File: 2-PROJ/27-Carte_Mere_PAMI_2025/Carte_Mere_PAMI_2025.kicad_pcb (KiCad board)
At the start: 2 copper layers, 212.2 x 114.8 mm, 114 parts, among them J1 Conn_01x03, J10 Conn_01x04, J11 Conn_01x03, J12 Conn_01x03, J13 Conn_01x03, J14 Conn_01x03, J15 3.5mm WR-TBL, J16 Conn_01x04, J17 Conn_01x02, J18 Conn_01x02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

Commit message: préplacement carte PAMI 2025
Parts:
- removed the H1 at (216.0, 73.0)
- removed the H2 at (250.6, 73.0)
- removed the H3 at (268.7, 23.7)
- removed the H4 at (197.7, 23.7)
- removed the J1 at (242.1, 83.1)
- C22: footprint Capacitor_THT:C_Radial_D8.0mm_H11.5mm_P3.50mm -> Capacitor_THT:C_Radial_D6.3mm_H11.0mm_P2.50mm
- J10, J2, J9: moved to B.Cu
- J15, J7: value 3.5mm WR-TBL -> Conn_01x02; footprint ConnectorsEvo:691321100002 -> Connector_Wire:SolderWire-0.75sqmm_1x02_P4.8mm_D1.25mm_OD2.3mm; moved to B.Cu
- J17, J18, J19, J3: footprint Connector_PinHeader_2.54mm:PinHeader_1x03_P2.54mm_Vertical -> Connector_PinHeader_2.54mm:PinHeader_1x02_P2.54mm_Vertical
- J8: footprint Connector_PinHeader_2.54mm:PinHeader_1x04_P2.54mm_Vertical -> Carte_Mere_PAMI_2025:Ecran_OLED0.9_Waveshare
- SW1: footprint Connector_PinHeader_2.54mm:PinHeader_1x03_P2.54mm_Vertical -> Button_Switch_THT:SW_Slide_SPDT_Straight_CK_OS102011MS2Q
- moved C21 145.2 mm to (150.0, 132.5), turned to 90 degrees
- moved U5 138.7 mm to (150.7, 113.9)
- moved J13 130.7 mm to (133.5, 129.0)
- moved J14 129.2 mm to (136.1, 129.0)
- moved J10 128.9 mm to (147.7, 115.7)
- moved C25 127.9 mm to (140.0, 125.0), turned to 180 degrees
- moved R20 125.1 mm to (140.0, 123.5)
- moved R21 124.4 mm to (140.0, 122.0), turned to 180 degrees
- moved R22 123.8 mm to (140.0, 120.5), turned to 180 degrees
- moved C15 121.1 mm to (152.7, 117.9), turned to 180 degrees
- moved J16 118.6 mm to (140.0, 108.0)
- moved C20 117.3 mm to (115.0, 132.0), turned to 90 degrees
- moved C27 117.2 mm to (128.0, 132.5), turned to 90 degrees
- moved C9 114.3 mm to (129.0, 95.5), turned to 90 degrees
- moved C23 113.2 mm to (143.0, 131.0), turned to 90 degrees
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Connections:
- D1 pad 1: Net-(D1-K) -> GND
- D1 pad 2: +5P -> Net-(D1-A)
- J17 pad 1: /uSW1 -> GND
- J17 pad 2: GND -> /uSW1
- J18 pad 1: /uSW2 -> GND
- J18 pad 2: GND -> /uSW2
- J19 pad 1: /uSW3 -> GND
- J19 pad 2: GND -> /uSW3
- J2 pad 1: /ALIM_EN_5L -> +5L
- J2 pad 2: /EN_5L -> GND
- J2 pad 3: /CaptTOR_2 -> GND
- J2 pad 4: /CaptTOR_1 -> +5P
- J2 pad 5: +5P -> /CaptTOR_1
- J2 pad 6: GND -> /CaptTOR_2
- J2 pad 7: GND -> /EN_5L
- J2 pad 8: +5L -> /ALIM_EN_5L
- J3 pad 1: +5P -> Net-(D2-A)
- J3 pad 2: Net-(D2-A) -> +5P
- R1 pad 1: GND -> Net-(D1-A)
- R1 pad 2: Net-(D1-K) -> +5P
- SW1 pad 1: unconnected-(SW1-C-Pad1) -> /ALIM_EN_5L
- SW1 pad 3: /ALIM_EN_5L -> /EN_5L
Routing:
- removed copper zone on B.Cu, net (none)
- removed copper zone on F.Cu, net (none)
- removed copper zone on B.Cu, net GND
- removed copper zone on F.Cu, net GND
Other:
- board size 212.2 x 114.8 mm -> 100 x 77 mm

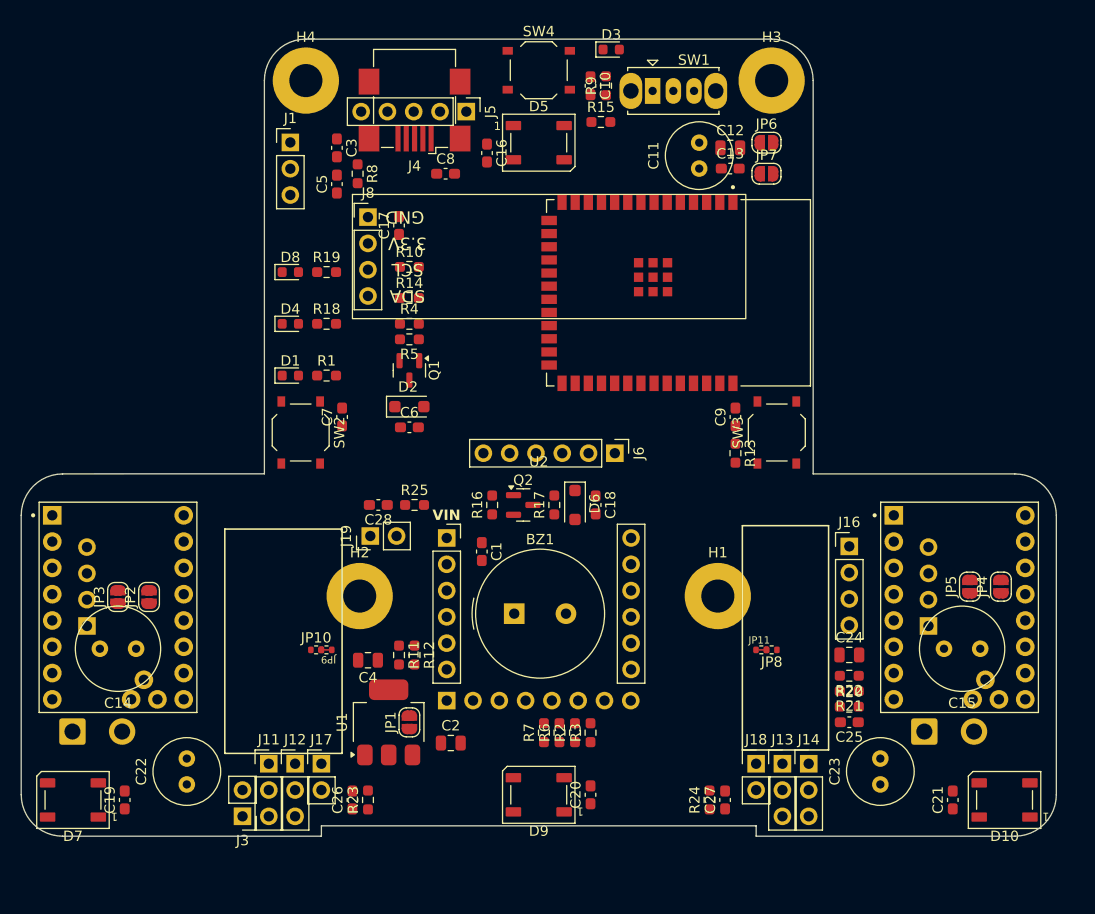
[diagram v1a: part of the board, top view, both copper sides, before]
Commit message: WIP routage avec ajout d'un AU_STATUS à la place de la LED statut
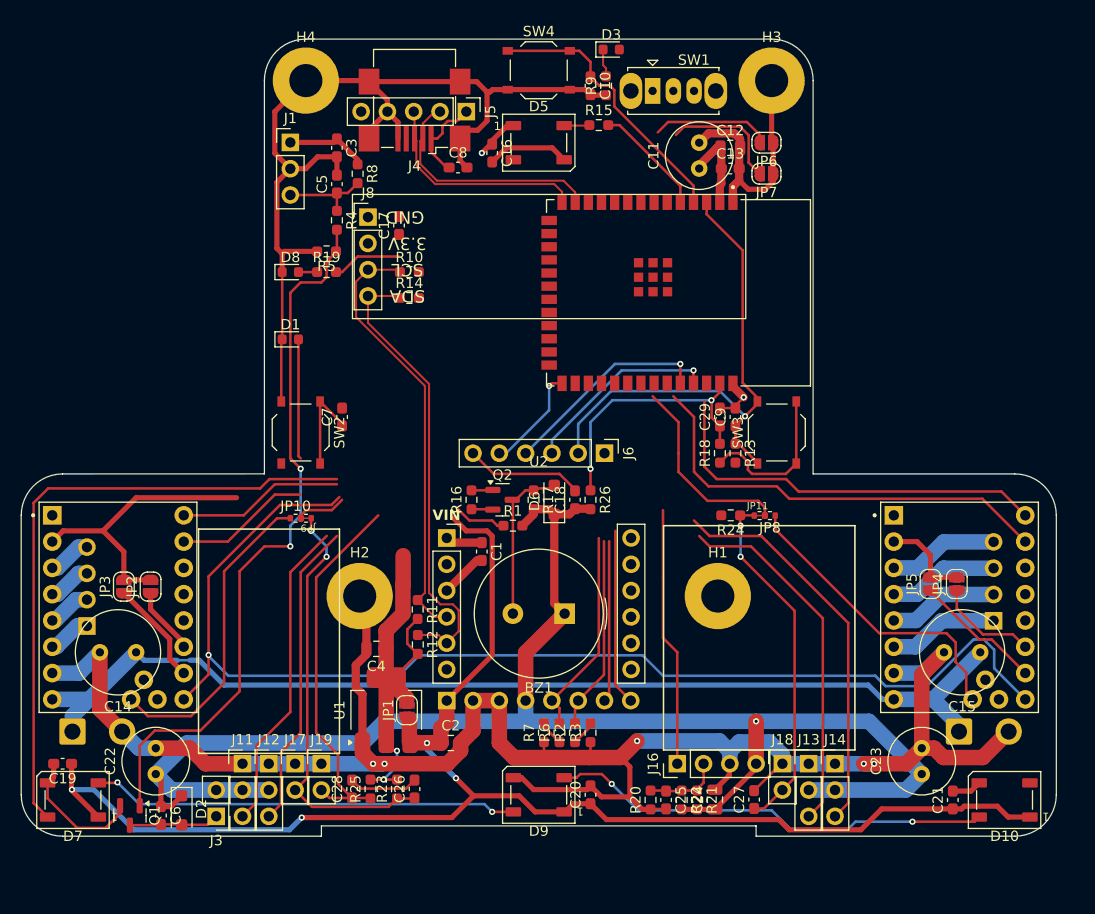
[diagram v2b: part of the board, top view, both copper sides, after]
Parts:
- removed D4: LED, LED_SMD:LED_0603_1608Metric
- added C29: 100nF, Capacitor_SMD:C_0603_1608Metric_Pad1.08x0.95mm_HandSolder, F.Cu at (127.5, 95.5)
- added R26: 10k, Resistor_SMD:R_0603_1608Metric_Pad0.98x0.95mm_HandSolder, F.Cu at (115.0, 103.5)
- J10, J9: footprint Connector_PinHeader_2.54mm:PinHeader_1x04_P2.54mm_Vertical -> Connector_PinHeader_2.54mm:PinHeader_1x04_P2.54mm_Horizontal
- R18: value 1K -> 10k
- moved Q1 50.8 mm to (70.5, 134.0)
- moved D2 44.8 mm to (75.5, 133.5), turned to -90 degrees
- moved C6 44.5 mm to (73.5, 134.0), turned to -90 degrees
- moved R18 40.0 mm to (127.5, 99.0), turned to 90 degrees
- moved R25 27.8 mm to (93.7, 131.4), turned to 90 degrees
- moved R24 27.6 mm to (128.5, 105.0), turned to 180 degrees
- moved C28 27.6 mm to (92.0, 131.4), turned to 90 degrees
- moved J16 26.8 mm to (123.4, 129.0), turned to 90 degrees
- moved R1 23.1 mm to (107.5, 106.0)
- moved J19 22.5 mm to (89.0, 129.0), turned to 0 degrees
- moved R20 21.2 mm to (120.8, 132.5), turned to 90 degrees
- moved R22 20.2 mm to (123.8, 132.5), turned to -90 degrees
- moved C25 19.2 mm to (122.3, 132.5), turned to -90 degrees
- moved C24 19.1 mm to (127.0, 132.5), turned to 90 degrees
- moved R21 18.1 mm to (125.3, 132.5), turned to -90 degrees
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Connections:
- net /LED_GREEN renamed /AU_STATUS
- R18 pad 1: Net-(D4-A) -> GND
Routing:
- net GND: track 0.00 -> 368.6 mm, vias 0 -> 6
- net +5P: track 0.00 -> 150.4 mm, vias 0 -> 1
- net +5L: track 0.00 -> 148.6 mm, vias 0 -> 5
- net /M_EN: track 0.00 -> 116.0 mm, vias 0 -> 1
- net VBATT_12V: track 0.00 -> 103.2 mm
- net +3.3V: track 0.00 -> 93.9 mm, vias 0 -> 2
- net Net-(Q1-G): track 0.00 -> 69.6 mm, vias 0 -> 2
- net /WS_2: track 0.00 -> 61.2 mm
- net /ESP32_EN: track 0.00 -> 50.5 mm, vias 0 -> 1
- net /SDA: track 0.00 -> 44.6 mm
- net /M2_STEP: track 0.00 -> 42.9 mm
- net /WS_4: track 0.00 -> 42.9 mm, vias 0 -> 2
- net /SCL: track 0.00 -> 42.1 mm
- net /WS_3: track 0.00 -> 41.3 mm, vias 0 -> 2
- net /uSW1: track 0.00 -> 40.7 mm, vias 0 -> 2
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
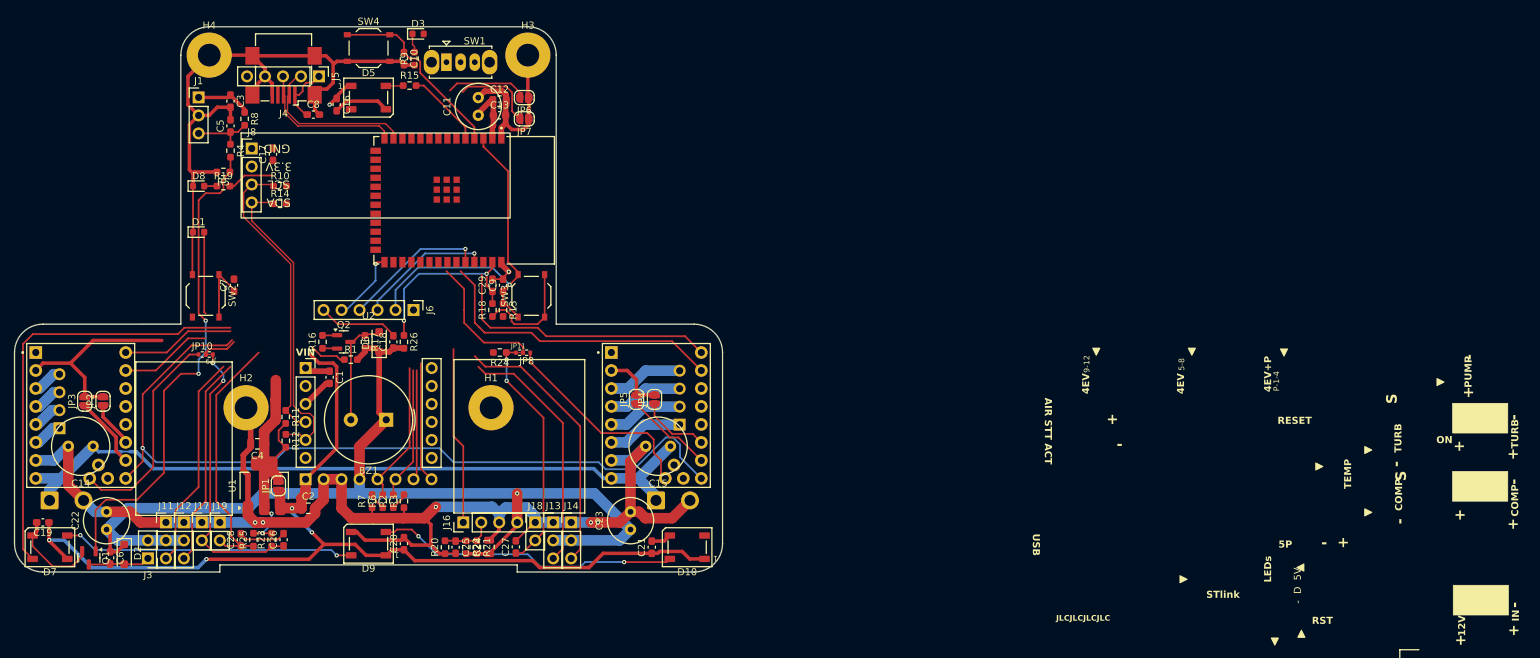
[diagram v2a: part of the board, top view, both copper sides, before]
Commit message: fin du routage carte PAMI 2025
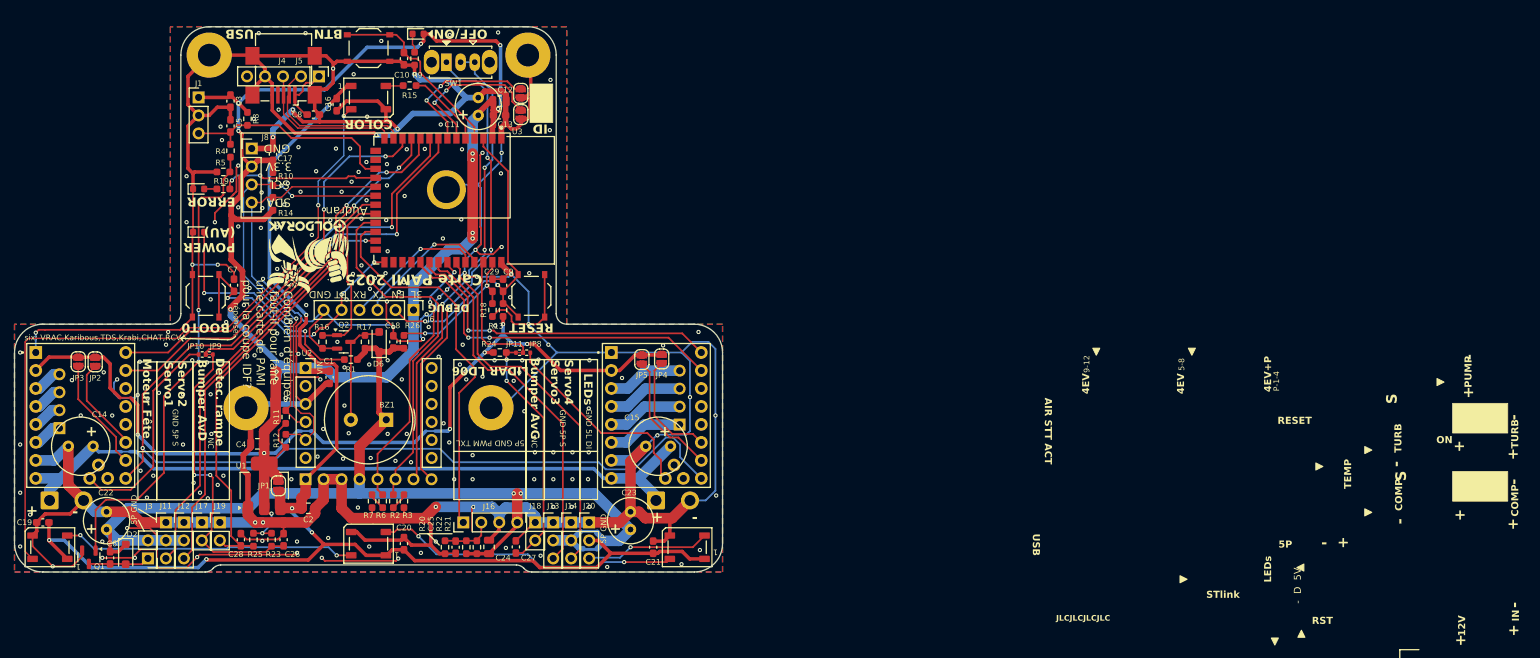
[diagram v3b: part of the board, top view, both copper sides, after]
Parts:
- added G***: LOGO, LOGO, F.Cu at (101.5, 92.5)
- added G***: LOGO, LOGO, F.Cu at (101.3, 87.1)
- added J20: Conn_01x03, Connector_PinHeader_2.54mm:PinHeader_1x03_P2.54mm_Vertical, F.Cu at (141.2, 129.0)
- moved JP4 5.82 mm to (151.4, 105.9)
- moved JP5 5.68 mm to (148.6, 106.0)
- moved JP2 5.68 mm to (71.4, 106.3)
- moved JP3 5.66 mm to (69.0, 106.3)
- moved R10 1.41 mm to (96.5, 80.5), turned to 90 degrees
- moved R14 1.00 mm to (96.5, 84.0), turned to -90 degrees
- moved JP6 0.78 mm to (131.5, 68.4), turned to 90 degrees
- moved JP7 0.78 mm to (131.5, 71.4), turned to 90 degrees
- moved D8 0.40 mm to (86.0, 81.9)
- moved R19 0.40 mm to (89.5, 81.9)
- moved R8 0.40 mm to (92.9, 72.0)
- moved D2 0.20 mm to (75.7, 133.5)
- moved C21 0.20 mm to (150.2, 132.5)
- moved Q1 0.08 mm to (70.5, 133.9)
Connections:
- D10 pad 2: unconnected-(D10-DOUT-Pad2) -> /WS_5
- U3 pad 18: /TX_LIDAR -> /LED_RED
- U3 pad 24: /M1_DIAG/uSW1 -> /TX_LIDAR
- U3 pad 38: /LED_RED -> /M2_DIAG/uSW2
- U3 pad 8: /M2_DIAG/uSW2 -> /M1_DIAG/uSW1
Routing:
- net GND: track 368.6 -> 790.3 mm, vias 6 -> 209
- net +3.3V: track 93.9 -> 346.7 mm, vias 2 -> 21
- net /EN_5L: track 15.6 -> 66.6 mm, vias 0 -> 3
- net /ALIM_EN_5L: track 17.0 -> 67.5 mm, vias 0 -> 3
- net /M1_DIAG/uSW1: track 4.90 -> 51.2 mm, vias 0 -> 2
- net +5L: track 148.6 -> 194.5 mm, vias 5 -> 6
- net /SERVO1: track 30.5 -> 76.0 mm, vias 0 -> 2
- net /M1_DIR: track 16.0 -> 59.8 mm, vias 0 -> 2
- net /SERVO2: track 29.8 -> 73.3 mm, vias 0 -> 2
- net /M_EN: track 116.0 -> 158.3 mm, vias 1 -> 3
- net /WS_2: track 61.2 -> 98.7 mm, vias 0 -> 2
- net /CaptTOR_2: track 18.7 -> 51.6 mm
- net /M1_STEP: track 13.2 -> 42.9 mm, vias 0 -> 2
- net /TX_LIDAR: track 25.1 -> 54.5 mm
- net /uSW3: track 36.3 -> 65.1 mm
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- added copper zone on B.Cu, net GND
- added copper zone on F.Cu, net GND
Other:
- outline, holes or cut-outs redrawn
- board text added: "3L EN TX RX BT GND"
- board text added: "5-36V"
- board text added: "5P GND"
- board text added: "5P GND PWM TXL"
- board text added: "<= Glory hole"
- board text added: "Audran"
- board text added: "BOOT0"
- board text added: "BTN"
- board text added: "Bumper AvD"
- board text added: "Bumper AvG"
- board text added: "COLOR"
- board text added: "Carte PAMI 2025"
- board text added: "Combien d'équipes faut-il pour faire une carte de PAMI pour la coupe IDF?"
- board text added: "DEBUG"
- board text added: "Detec. rampe"
- board text added: "EN_5L Cp2 Cp1 +5P GND GND +5L"
- board text added: "ERROR"
- board text added: "GND 5L DI"
- board text added: "GND 5P S"
- board text added: "ID"
- board text added: "LIDAR LD06"
- board text added: "M1B M1A M2A M2B"
- board text added: "MOT Droit"
- board text added: "MOT Gauche"
- board text added: "Moteur Fête"
- board text added: "NC"
- board text added: "OFF/ON"
- board text added: "POWER (AU)"
- board text added: "Servo2 Servo1"
- board text added: "Servo4 Servo3"
- board text added: "réponse:"
- board text added: "six: VRAC,Karibous,TDS,Krabi,CHAT,RCVA"
- board text removed: "Carte Pneumatique 2025"
- board text removed: "Mehdi, Raphael & Audran"

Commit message: modification de bouton et fichier de prod
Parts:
- added SW5: SW_Push, Button_Switch_SMD:SW_Push_1TS009xxxx-xxxx-xxxx_6x6x5mm, F.Cu at (86.9, 97.0)
- added SW6: SW_Push, Button_Switch_SMD:SW_Push_1TS009xxxx-xxxx-xxxx_6x6x5mm, F.Cu at (133.0, 97.0)
- added SW7: SW_Push, Button_Switch_SMD:SW_Push_1TS009xxxx-xxxx-xxxx_6x6x5mm, F.Cu at (110.0, 62.3)
- D1: value LED -> LED yellow
- D3: value LED -> LED green
- D8: value LED -> LED red
- R1, R17, R19, R9: value 1K -> 1k
- R10, R11, R12, R13, R14, R20, R21, R22, R23, R24, R25: value 10K -> 10k
- moved J9 0.53 mm to (66.3, 115.2)
- moved SW4 0.30 mm to (110.0, 62.3)
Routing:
- net GND: track 790.3 -> 803.5 mm, vias 209 -> 211
- net /BOOT0: track 40.7 -> 42.7 mm
- net Net-(D1-A): track 33.4 -> 31.5 mm
- net /ESP32_EN: track 48.1 -> 50.0 mm
- net /COLORSIDE: track 26.7 -> 28.5 mm
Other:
- outline, holes or cut-outs redrawn
- board text removed: "- D 5V"
- board text removed: "12V"
- board text removed: "4EV"
- board text removed: "4EV+P"
- board text removed: "5-8"
- board text removed: "5P"
- board text removed: "9-12"
- board text removed: "AIR STT ACT"
- board text removed: "AU/CAN"
- board text removed: "COMP"
- board text removed: "Cent versions plus tard, nous l'avons enfin soudée. Et même si sa maitrise de l'air est exceptionnelle, elle a encore des timing à affiner avant de pouvoir sauver nos actionneurs."
- board text removed: "IN"
- board text removed: "JLCJLCJLCJLC"
- board text removed: "L'eau, la terre, le feu, l'air. Il y a très longtemps, ces quatre éléments vivaient en harmonie dans l'atelier."
- board text removed: "Mais j'en suis sûr : cette carte peut sauver notre robot."
- board text removed: "Mais juste au moment où on avait besoin d'elle… elle était encore en phase de prototypage."
- board text removed: "Mais un jour, la magic smoke décida de s'échapper."
- board text removed: "ON"
- board text removed: "P-1-4"
- board text removed: "PUMP"
- board text removed: "RST"
- board text removed: "S"
- board text removed: "STlink"
- board text removed: "Seule la carte pneumatique, maîtresse des électrovannes et du compresseur, pouvait rétablir l'équilibre."
- board text removed: "TEMP"
- board text removed: "TURB"
